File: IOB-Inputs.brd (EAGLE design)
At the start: 53.3 x 20.3 mm, 20 parts, among them J1 RJ12/6

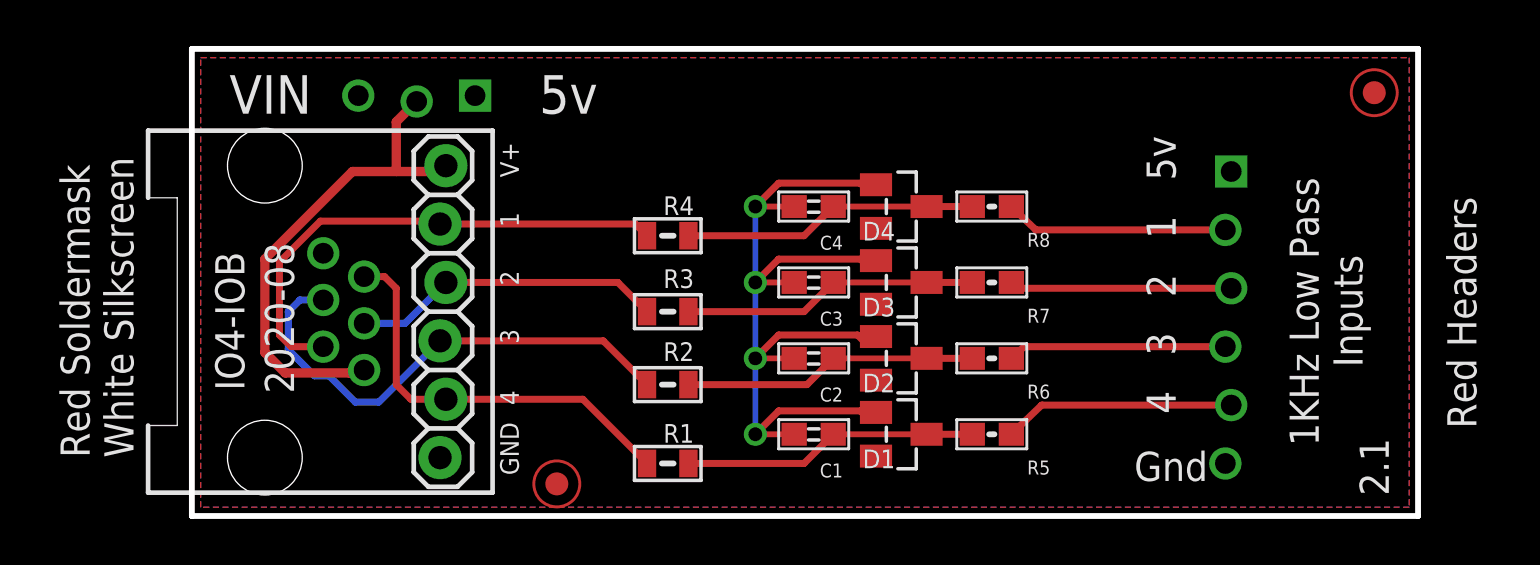
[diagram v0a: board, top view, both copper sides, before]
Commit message: Moved 82R inline with others
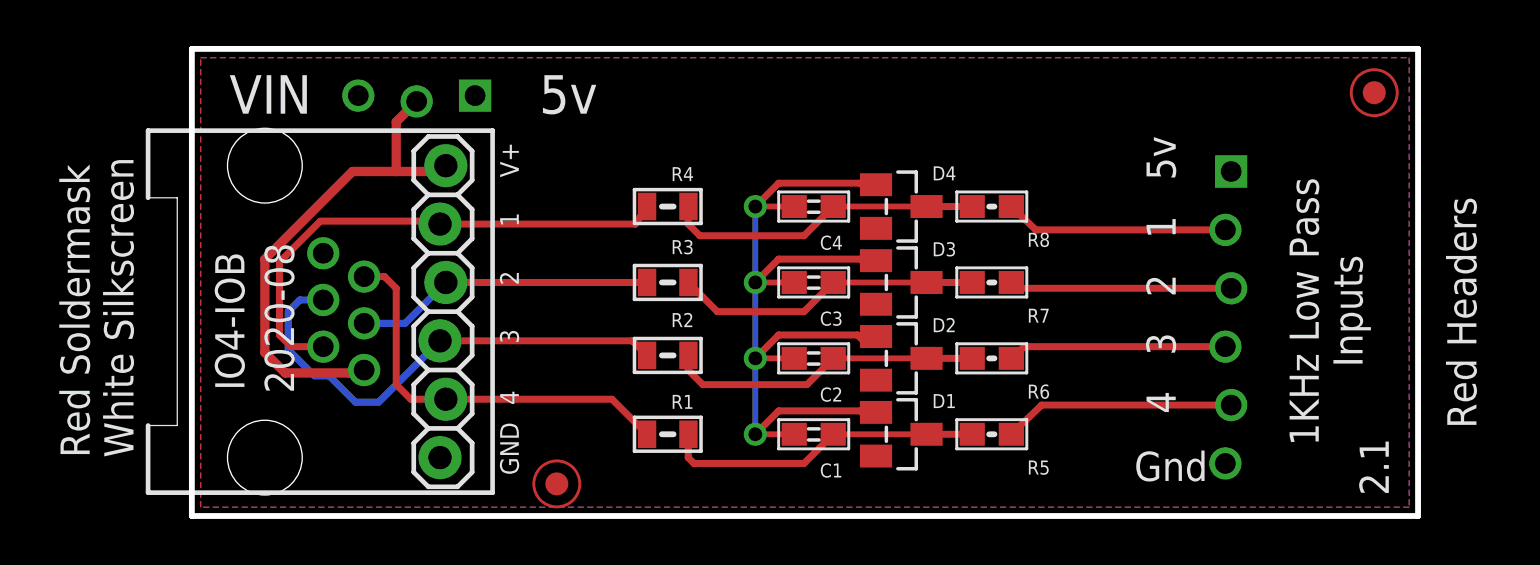
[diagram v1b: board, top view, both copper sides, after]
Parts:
- moved R2 1.27 mm to (20.7, 6.99)
- moved R1 1.27 mm to (20.7, 3.56)
- moved R3 1.27 mm to (20.7, 10.2)
- moved R4 1.27 mm to (20.7, 13.5)
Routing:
- net N$10: track 12.9 -> 14.0 mm
- net N$14: track 12.9 -> 13.9 mm
- net N$12: track 12.8 -> 13.7 mm
- net N$13: track 12.9 -> 13.4 mm
- net !IO4: track 18.1 -> 17.6 mm
- net !IO3: track 21.8 -> 21.3 mm
- net !IO2: track 13.6 -> 13.0 mm
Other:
- board text added: "R1"
- board text added: "R2"
- board text added: "R3"
- board text added: "R4"
- board text removed: "R10"
- board text removed: "R11"
- board text removed: "R12"
- board text removed: "R9"
